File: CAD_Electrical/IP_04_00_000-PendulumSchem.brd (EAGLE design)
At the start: 160 x 100 mm, 7 parts

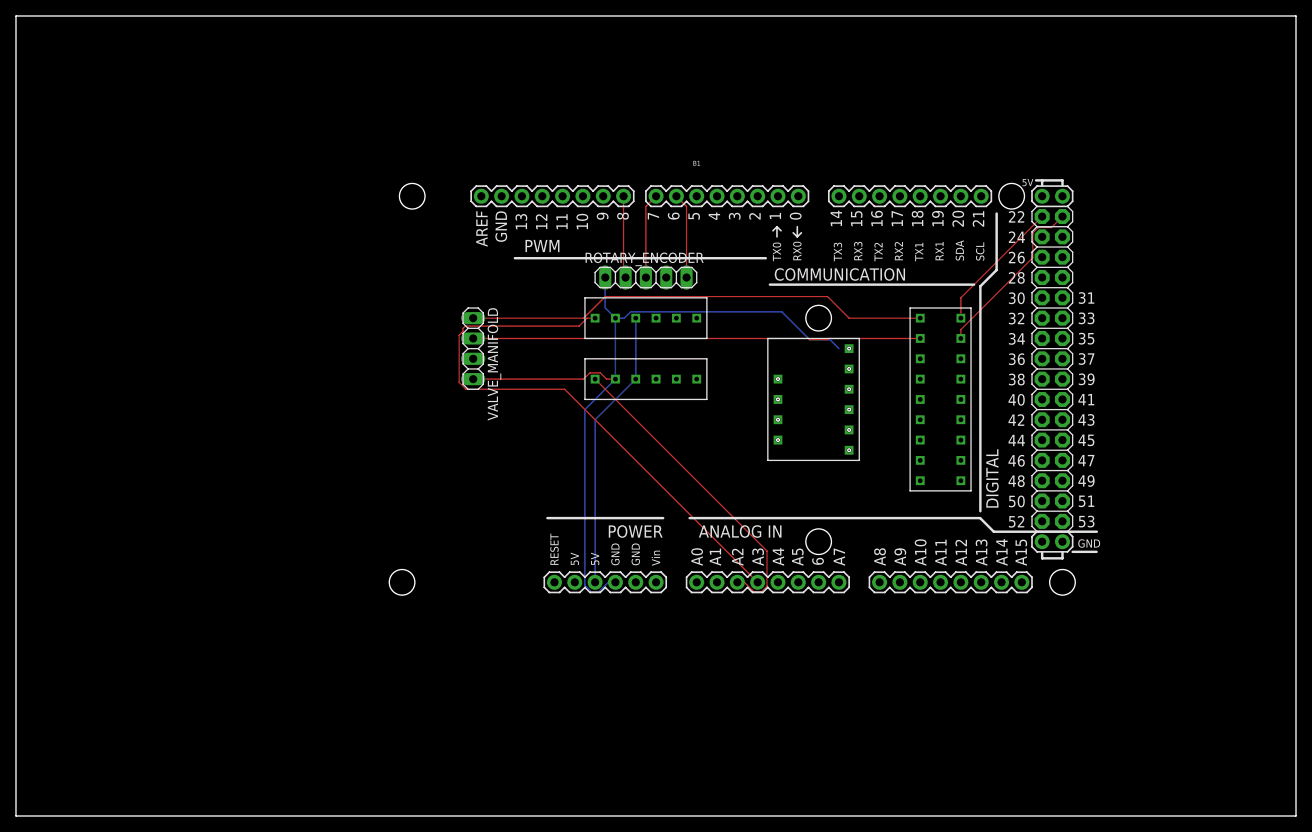
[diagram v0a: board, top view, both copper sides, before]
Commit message: Fixed shape of pins on PCB shield
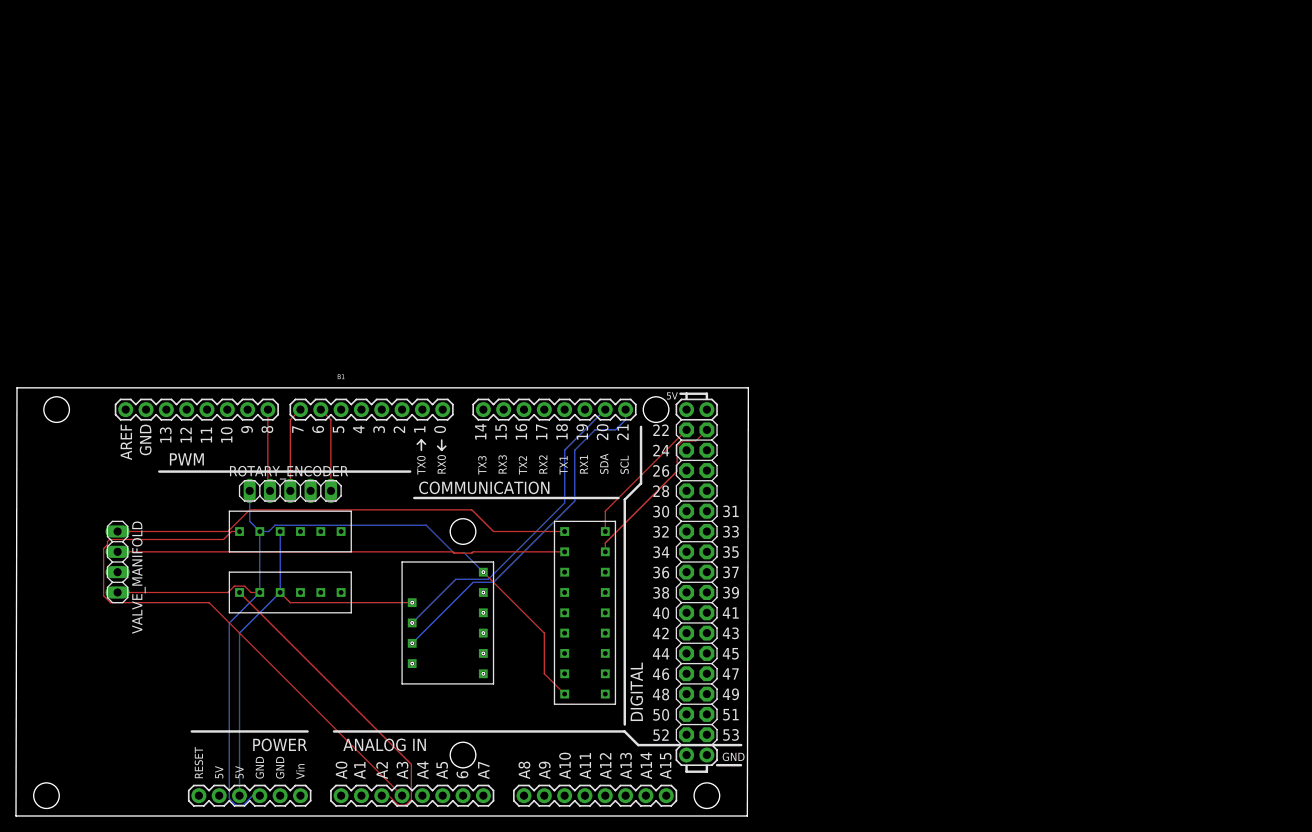
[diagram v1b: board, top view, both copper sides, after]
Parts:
- moved U$1 53.6 mm to (55.9, 22.9)
- moved B1 51.8 mm to (39.4, 26.7)
- moved ROTARY_ENCODER 51.8 mm to (34.3, 40.6)
- moved U$2 51.8 mm to (73.7, 35.6)
- moved U$3 51.8 mm to (27.9, 27.9)
- moved U$4 51.8 mm to (27.9, 35.6)
- moved VALVE_MANIFOLD 51.8 mm to (12.7, 31.8)
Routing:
- net N$7: track 0.00 -> 43.2 mm
- net N$3: track 0.00 -> 39.0 mm
- net GND: track 93.8 -> 113.8 mm
- net +5V: track 35.1 -> 52.2 mm
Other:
- board size 160 x 100 mm -> 91.5 x 53.5 mm
